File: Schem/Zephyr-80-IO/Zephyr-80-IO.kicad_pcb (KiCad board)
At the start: 6 copper layers, 160 x 64.4 mm, 91 parts, among them IC1 Z80CTC, IC2 Z80SIO, IC3 Z80SIO, J1 pBITzBus, J2 548190519, J3 L77HDA26SD1CH4F, J5 Conn_01x08_Pin, SW1 SW_Push, SW2 SW_Push, SW3 SW_Coded_SH-7070, SW4 SW_Coded_SH-7070, SW5 SW_Coded_SH-7070, SW6 SW_Coded_SH-7070, SW7 SW_Coded_SH-7030, SW8 SW_Coded_SH-7030, U10 74HC688, U11 74HC688, U12 74HC688, U13 74HC244, U14 MAX202IDR, U15 PIC18F57Q84-I/PT, U2 74AHC1G125, U3 74AHC1G125, U4 74AHC595, U5 74AHC595, U6 74HC138, U7 FT230XS-U, U8 SN74HC4040DR, U9 74HC688, Y1 ECS-2100AX-147.4

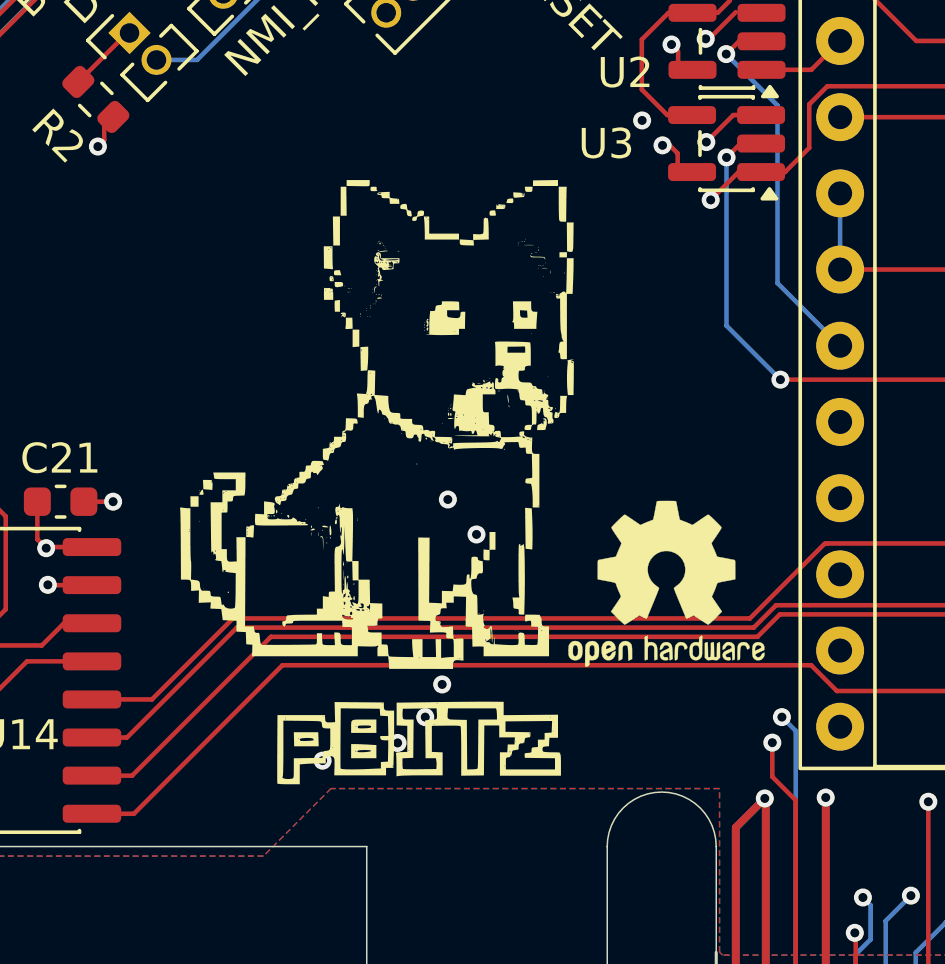
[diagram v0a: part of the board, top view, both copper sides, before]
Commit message: Added Zephyr-80 Logo
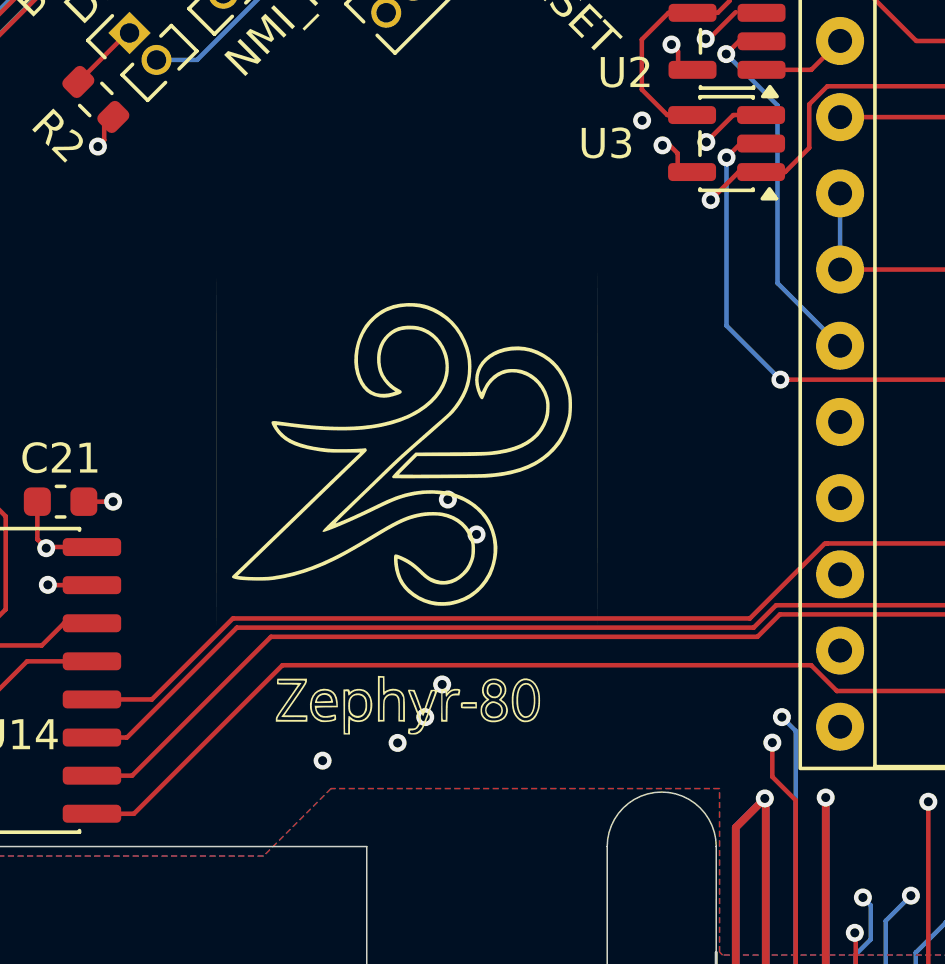
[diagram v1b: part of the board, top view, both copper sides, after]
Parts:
- added G***: LOGO, Footprints:zephir-80-Silk, F.Cu at (111.2, 93.6)
- G***, REF**: moved to B.Cu
- moved REF** 17.4 mm to (102.9, 102.0), turned to 180 degrees
- turned G*** to 180 degrees

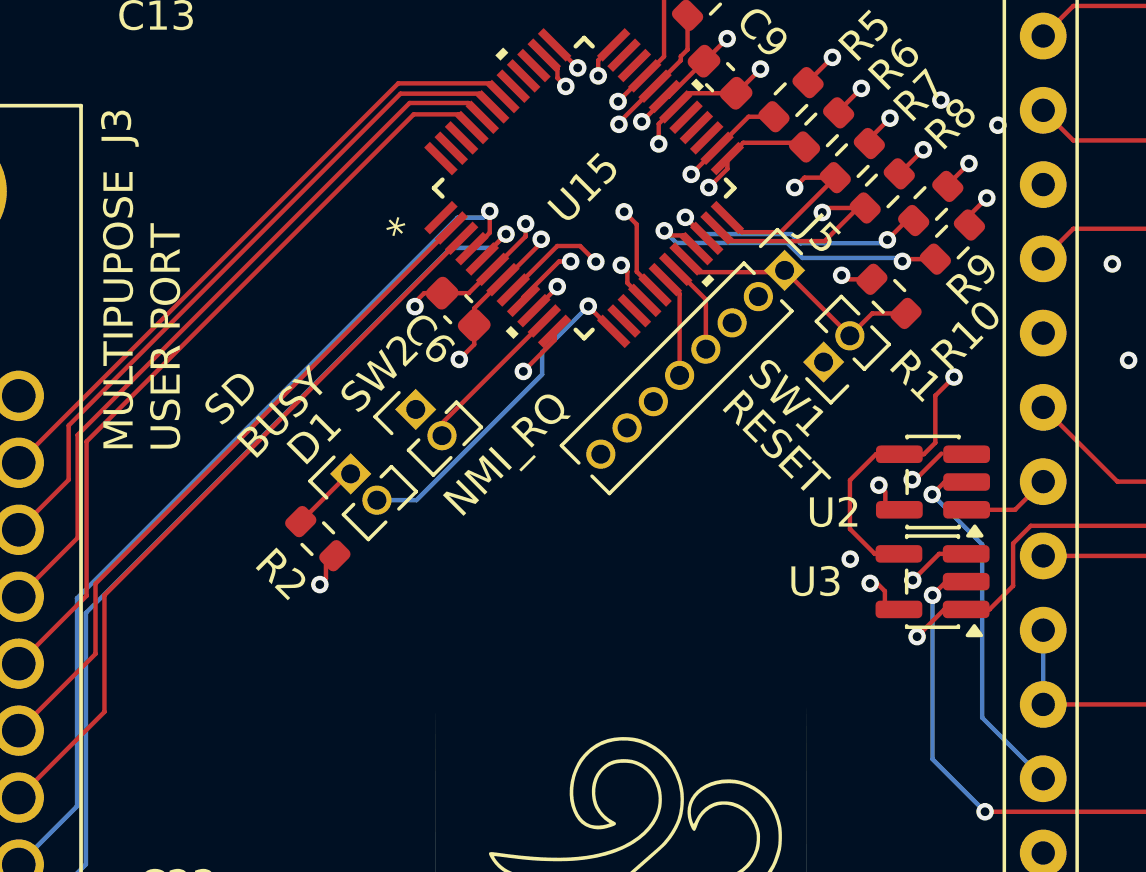
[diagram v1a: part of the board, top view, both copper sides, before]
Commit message: Fixed io controller 1.27mm pitch header to 2.54mm pitch header.
First battle scars :)
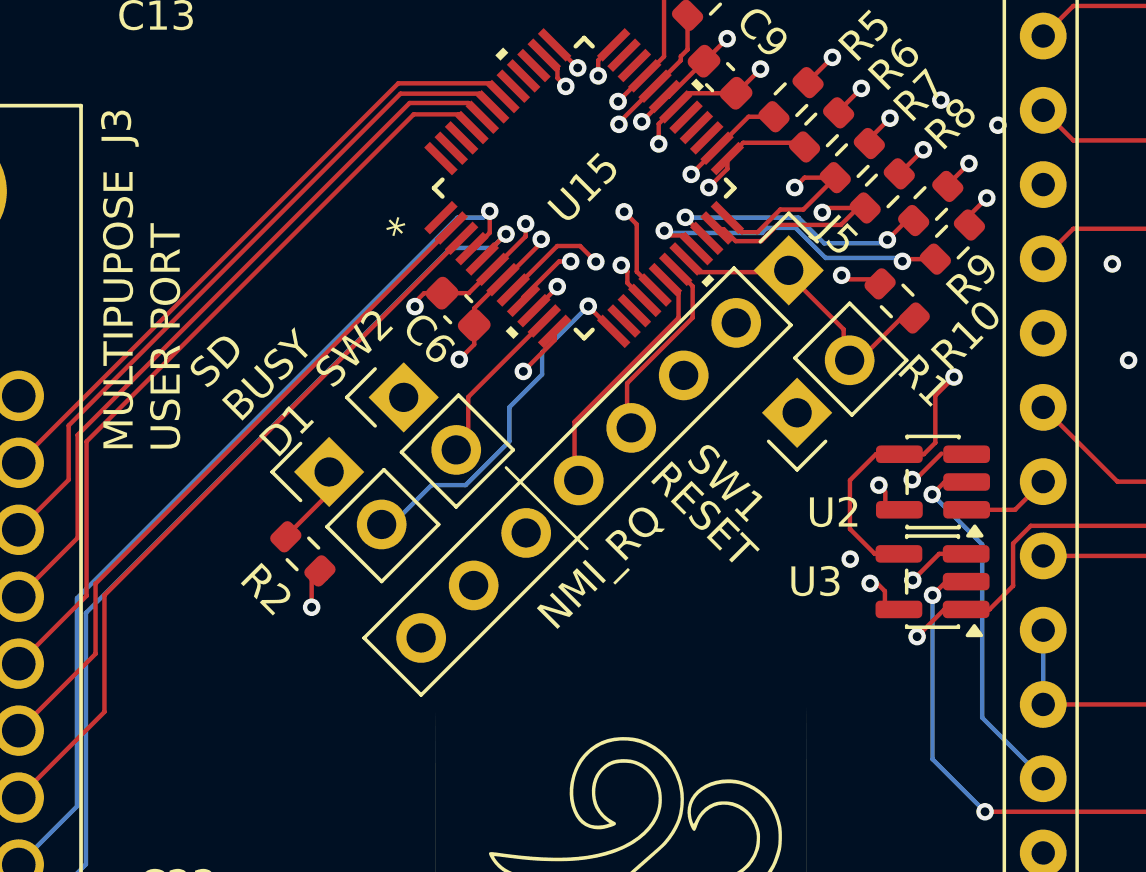
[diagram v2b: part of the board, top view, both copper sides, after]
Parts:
- D1, SW1, SW2: footprint Connector_PinHeader_1.27mm:PinHeader_1x02_P1.27mm_Vertical -> Connector_PinHeader_2.54mm:PinHeader_1x02_P2.54mm_Vertical
- J5: footprint Connector_PinHeader_1.27mm:PinHeader_1x08_P1.27mm_Vertical -> Connector_PinHeader_2.54mm:PinHeader_1x08_P2.54mm_Vertical
- moved SW1 1.96 mm to (117.2, 77.6)
- moved D1 0.74 mm to (101.2, 79.6)
- moved R2 0.73 mm to (100.3, 82.4)
- moved SW2 0.58 mm to (103.8, 77.1)
- moved R1 0.32 mm to (120.7, 73.8)
- moved J5 0.14 mm to (116.9, 72.7)
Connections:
- J1 pad B6: /pBITz Bus Interface/CLK_20M -> unconnected-(J1A-CLK1-PadB6)
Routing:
- net Net-(J5-Pin_5): track 3.48 -> 8.53 mm
- net Net-(J5-Pin_4): track 3.16 -> 6.59 mm
- net /IO Controller Card/MOSI: track 147.0 -> 148.8 mm
- net /IO Controller Card/~{SIO1B_INT}: track 66.3 -> 67.9 mm
- net /IO Controller Card/~{RESET}: track 265.8 -> 267.2 mm
- net /IO Controller Card/~{MCLR}: track 8.98 -> 10.3 mm
- net /IO Controller Card/SD_PRESENT: track 68.7 -> 69.6 mm
- net Net-(D1-K): track 2.38 -> 3.12 mm
- net GND: track 246.1 -> 246.7 mm
- net /IO Controller Card/~{NMI_RQ}: track 5.37 -> 5.90 mm
